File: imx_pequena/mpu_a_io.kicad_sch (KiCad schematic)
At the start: 26 parts, among them J1 Conn_ARM_JTAG_SWD_10, U1 MCIMX6Z0DVM09AB, Y1 Crystal, Y2 Crystal

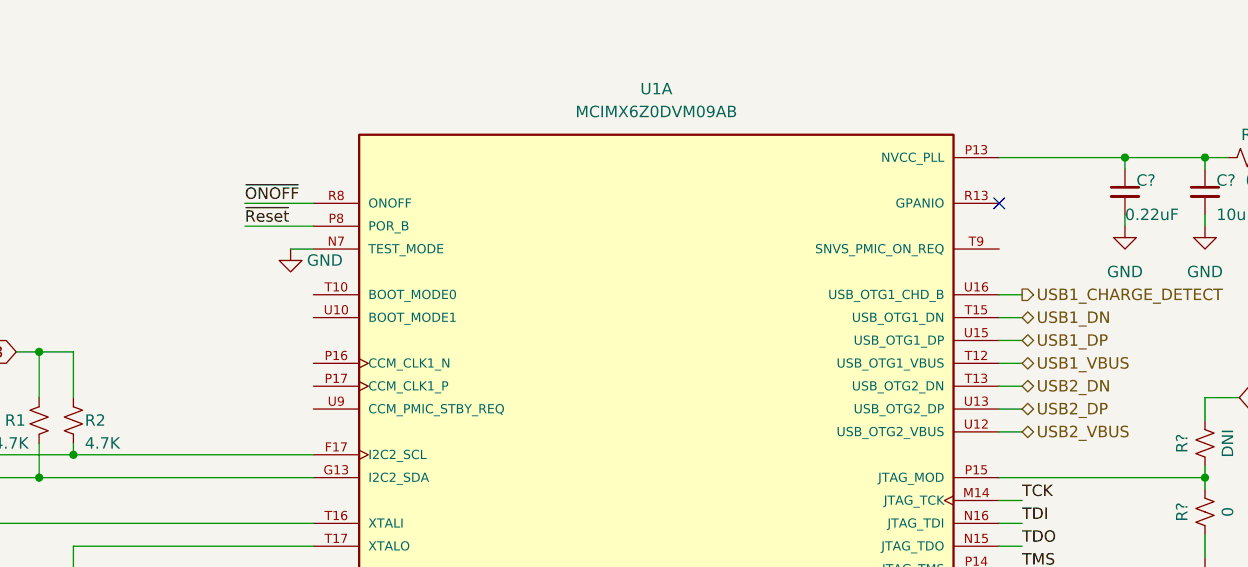
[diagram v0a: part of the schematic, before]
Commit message: Added test points
added test points
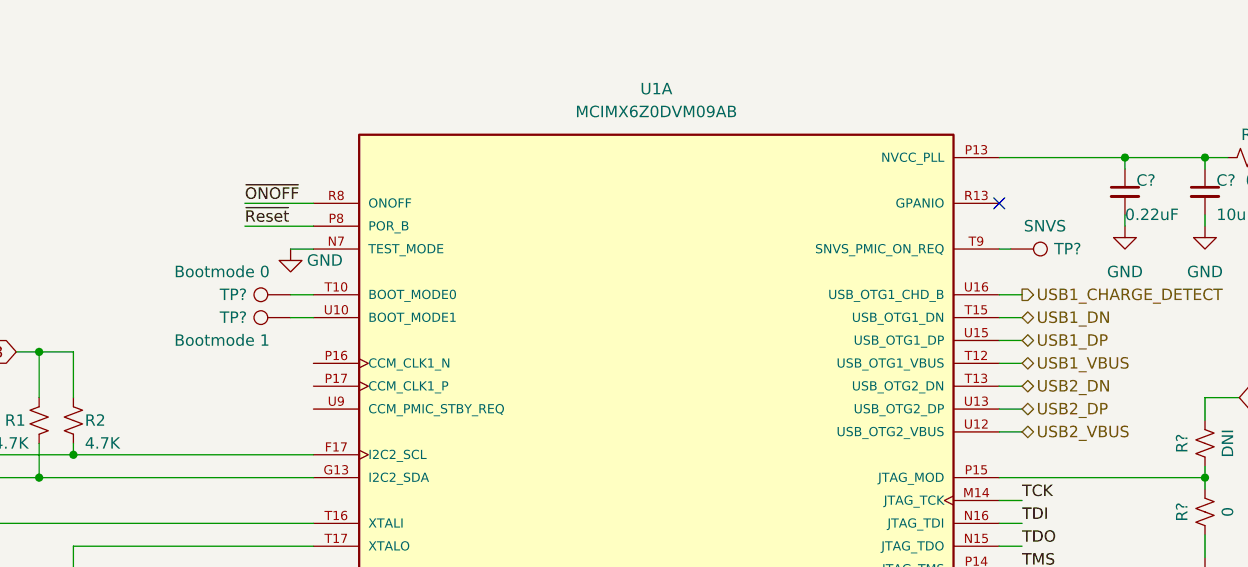
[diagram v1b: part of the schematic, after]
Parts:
- added TP?: Bootmode 0, symbol Connector:TestPoint
- added TP?: SNVS, symbol Connector:TestPoint
- added TP?: Bootmode 1, symbol Connector:TestPoint
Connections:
- net at U1.T10 (BOOT_MODE0): now also TP?.1
- net at U1.T9 (SNVS_PMIC_ON_REQ): now also TP?.1
- net at U1.U10 (BOOT_MODE1): now also TP?.1
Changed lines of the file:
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@@
+    (stroke (width 0) (type default) (color 0 0 0 0))
+  )
+  (wire (pts (xy 106.68 73.66) (xy 109.22 73.66))
     (stroke (width 0) (type default) (color 0 0 0 0))
   )
@@
     (stroke (width 0) (type default) (color 0 0 0 0))
   )
+  (wire (pts (xy 106.68 76.2) (xy 109.22 76.2))
+    (stroke (width 0) (type default) (color 0 0 0 0))
+  )
   (wire (pts (xy 101.6 63.5) (xy 109.22 63.5))
     (stroke (width 0) (type default) (color 0 0 0 0))
@@
   )
   (wire (pts (xy 82.55 85.09) (xy 82.55 80.01))
+    (stroke (width 0) (type default) (color 0 0 0 0))
+  )
+  (wire (pts (xy 185.42 68.58) (xy 186.69 68.58))
     (stroke (width 0) (type default) (color 0 0 0 0))
   )
@@
     (pin "1")
   )
+  (symbol (lib_id "Connector:TestPoint") (at 106.68 73.66 90) (unit 1)
+    (in_bom yes) (on_board yes)
+    (property "Reference" "TP?" (id 0) (at 100.33 73.66 90))
+    (property "Value" "Bootmode 0" (id 1) (at 99.06 71.12 90))
+    (property "Footprint" "" (id 2) (at 106.68 68.58 0)
+      (effects (font (size 1.27 1.27)) hide)
+    )
+    (property "Datasheet" "~" (id 3) (at 106.68 68.58 0)
+      (effects (font (size 1.27 1.27)) hide)
+    )
+    (pin "1")
+  )
   (symbol (lib_id "power:GND") (at 45.72 49.53 0) (unit 1)
     (in_bom yes) (on_board yes) (fields_autoplaced)
@@
     (pin "1")
     (pin "2")
+  )
+  (symbol (lib_id "Connector:TestPoint") (at 186.69 68.58 270) (unit 1)
+    (in_bom yes) (on_board yes)
+    (property "Reference" "TP?" (id 0) (at 193.04 68.58 90))
+    (property "Value" "SNVS" (id 1) (at 190.5 66.04 90))
+    (property "Footprint" "" (id 2) (at 186.69 73.66 0)
+      (effects (font (size 1.27 1.27)) hide)
+    )
+    (property "Datasheet" "~" (id 3) (at 186.69 73.66 0)
+      (effects (font (size 1.27 1.27)) hide)
+    )
+    (pin "1")
   )
   (symbol (lib_id "Device:C") (at 93.98 119.38 0) (unit 1)
@@
     (pin "2")
   )
+  (symbol (lib_id "Connector:TestPoint") (at 106.68 76.2 90) (unit 1)
+    (in_bom yes) (on_board yes)
+    (property "Reference" "TP?" (id 0) (at 100.33 76.2 90))
+    (property "Value" "Bootmode 1" (id 1) (at 99.06 78.74 90))
+    (property "Footprint" "" (id 2) (at 106.68 71.12 0)
+      (effects (font (size 1.27 1.27)) hide)
+    )
+    (property "Datasheet" "~" (id 3) (at 106.68 71.12 0)
+      (effects (font (size 1.27 1.27)) hide)
+    )
+    (pin "1")
+  )
 )

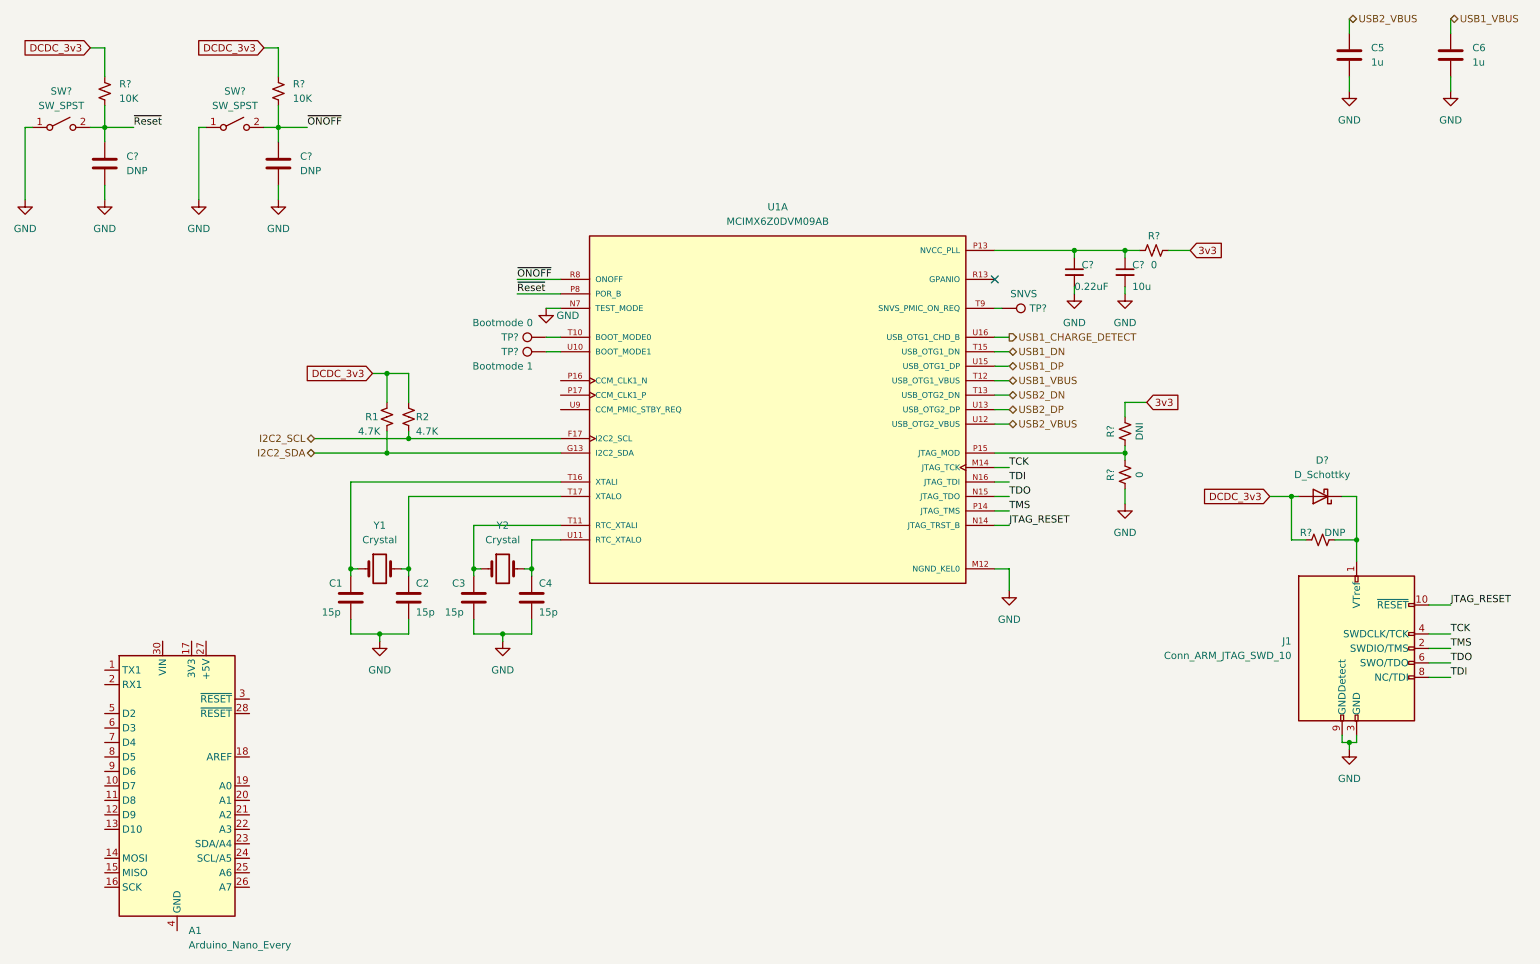
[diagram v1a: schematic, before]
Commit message: Part Assignment
Assigned GPIOs and assigned footprints to most parts
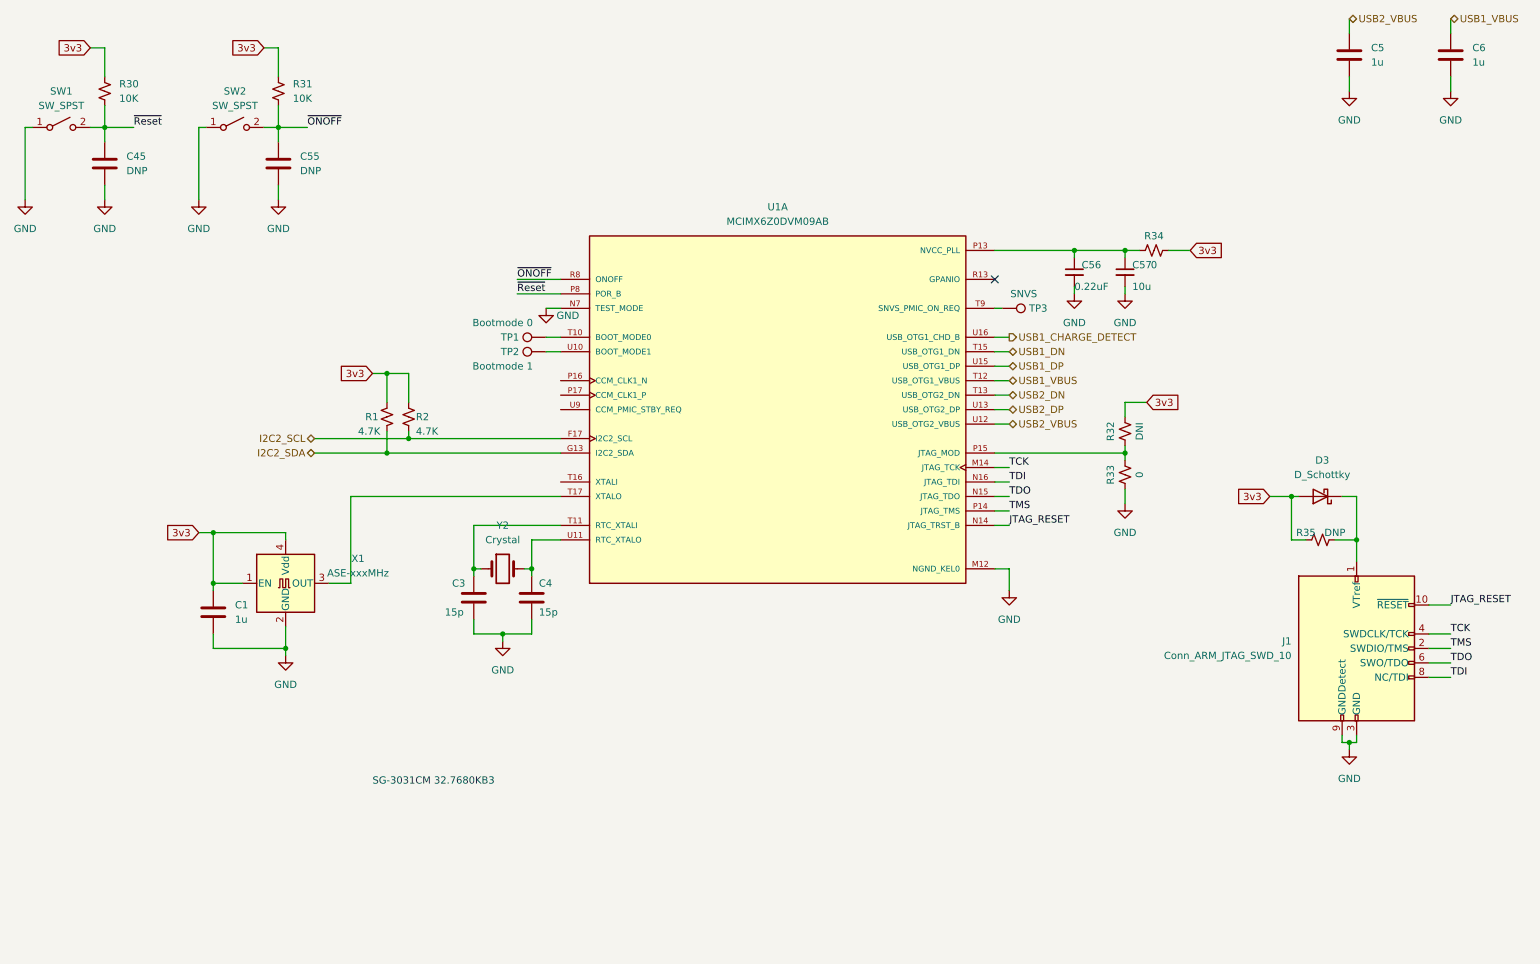
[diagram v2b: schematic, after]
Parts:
- removed A1: Arduino_Nano_Every, Module:Arduino_Nano, symbol MCU_Module:Arduino_Nano_Every
- removed C2: 15p, symbol Device:C
- removed Y1: Crystal, symbol Device:Crystal
- added X1: ASE-xxxMHz, Oscillator:Oscillator_SMD_Abracon_ASE-4Pin_3.2x2.5mm, symbol Oscillator:ASE-xxxMHz
- C1: value 15p -> 1u; footprint (none) -> Capacitor_SMD:C_0603_1608Metric
- C3, C4: footprint (none) -> Capacitor_SMD:C_0402_1005Metric
- C45, C56: renamed from C?; footprint (none) -> Capacitor_SMD:C_0402_1005Metric
- C5, C6: footprint (none) -> Capacitor_SMD:C_0603_1608Metric
- C55, C57: renamed from C?; footprint (none) -> Capacitor_SMD:C_0805_2012Metric
- D3: renamed from D?; footprint (none) -> Diode_SMD:D_SOD-123
- J1: footprint (none) -> Connector_PinHeader_1.27mm:PinHeader_2x05_P1.27mm_Vertical
- R1, R2: footprint (none) -> Resistor_SMD:R_0402_1005Metric
- R30, R31, R32, R33, R34, R35: renamed from R?; footprint (none) -> Resistor_SMD:R_0402_1005Metric
- SW1, SW2: renamed from SW?; footprint (none) -> Button_Switch_SMD:SW_SPST_TL3342
- TP1, TP2, TP3: renamed from TP?; footprint (none) -> TestPoint:TestPoint_Pad_1.0x1.0mm
- Y2: footprint (none) -> Crystal:Crystal_SMD_MicroCrystal_MS1V-T1K
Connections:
- net DCDC_3v3 is gone; now on net 3v3: D3.2 (A), R1.1, R2.1, R30.1, R31.1, R35.1
- net 3v3: now also C1.1, X1.1 (EN), X1.4 (Vdd)
- net GND: now also X1.2 (GND)
- net at U1.T17 (XTALO): now also X1.3 (OUT)
- net at U1.T16 (XTALI): no longer C1.1
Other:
- note added: "SG-3031CM 32.7680KB3"

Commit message: lots of updates
Set design rules, fixed ERC, etc....
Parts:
- J1: footprint Connector_PinHeader_1.27mm:PinHeader_2x05_P1.27mm_Vertical -> (none)
- Y2: footprint Crystal:Crystal_SMD_MicroCrystal_MS1V-T1K -> (none)
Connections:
- no-connect marks 1 -> 5
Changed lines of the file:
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@@
   (junction (at 247.65 144.78) (diameter 0) (color 0 0 0 0)
   )
+  (no_connect (at 100.33 86.36))
+  (no_connect (at 100.33 81.28))
+  (no_connect (at 100.33 83.82))
   (no_connect (at 185.42 63.5))
+  (no_connect (at 100.33 99.06))
   (wire (pts (xy 199.39 58.42) (xy 199.39 59.69))
     (stroke (width 0) (type default) (color 0 0 0 0))
@@
     (stroke (width 0) (type default) (color 0 0 0 0))
   )
+  (wire (pts (xy 100.33 83.82) (xy 109.22 83.82))
+    (stroke (width 0) (type default) (color 0 0 0 0))
+  )
   (wire (pts (xy 78.74 93.98) (xy 78.74 90.17))
     (stroke (width 0) (type default) (color 0 0 0 0))
@@
     (stroke (width 0) (type default) (color 0 0 0 0))
   )
+  (wire (pts (xy 100.33 86.36) (xy 109.22 86.36))
+    (stroke (width 0) (type default) (color 0 0 0 0))
+  )
   (wire (pts (xy 59.69 27.94) (xy 59.69 22.86))
     (stroke (width 0) (type default) (color 0 0 0 0))
@@
     (stroke (width 0) (type default) (color 0 0 0 0))
   )
+  (wire (pts (xy 100.33 81.28) (xy 109.22 81.28))
+    (stroke (width 0) (type default) (color 0 0 0 0))
+  )
   (wire (pts (xy 248.92 144.78) (xy 248.92 143.51))
     (stroke (width 0) (type default) (color 0 0 0 0))
@@
   )
   (wire (pts (xy 109.22 101.6) (xy 72.39 101.6))
+    (stroke (width 0) (type default) (color 0 0 0 0))
+  )
+  (wire (pts (xy 100.33 99.06) (xy 109.22 99.06))
     (stroke (width 0) (type default) (color 0 0 0 0))
   )
@@
     (property "Reference" "Y2" (id 0) (at 99.06 106.68 0))
     (property "Value" "Crystal" (id 1) (at 99.06 109.22 0))
-    (property "Footprint" "Crystal:Crystal_SMD_MicroCrystal_MS1V-T1K" (id 2) (at 99.06 114.3 0)
+    (property "Footprint" "" (id 2) (at 99.06 114.3 0)
       (effects (font (size 1.27 1.27)) hide)
     )
@@
       (effects (font (size 1.27 1.27)) (justify right))
     )
-    (property "Footprint" "Connector_PinHeader_1.27mm:PinHeader_2x05_P1.27mm_Vertical" (id 2) (at 248.92 128.27 0)
-      (effects (font (size 1.27 1.27)) hide)
-    )
+    (property "Footprint" "" (id 2) (at 248.92 128.27 0)
+      (effects (font (size 1.27 1.27)) hide)
+    )

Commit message: fixed part alllocation
fixed socket to pin header issue
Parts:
- J1: footprint (none) -> Connector_PinHeader_1.27mm:PinHeader_2x05_P1.27mm_Vertical
- Y2: footprint (none) -> Crystal:Crystal_SMD_MicroCrystal_MS1V-T1K
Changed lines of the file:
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@@
     (property "Reference" "Y2" (id 0) (at 99.06 106.68 0))
     (property "Value" "Crystal" (id 1) (at 99.06 109.22 0))
-    (property "Footprint" "" (id 2) (at 99.06 114.3 0)
+    (property "Footprint" "Crystal:Crystal_SMD_MicroCrystal_MS1V-T1K" (id 2) (at 99.06 114.3 0)
       (effects (font (size 1.27 1.27)) hide)
     )
@@
       (effects (font (size 1.27 1.27)) (justify right))
     )
-    (property "Footprint" "" (id 2) (at 248.92 128.27 0)
+    (property "Footprint" "Connector_PinHeader_1.27mm:PinHeader_2x05_P1.27mm_Vertical" (id 2) (at 248.92 128.27 0)
       (effects (font (size 1.27 1.27)) hide)
     )
